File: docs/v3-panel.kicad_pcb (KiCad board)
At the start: 2 copper layers, 20 x 128.5 mm, 0 parts

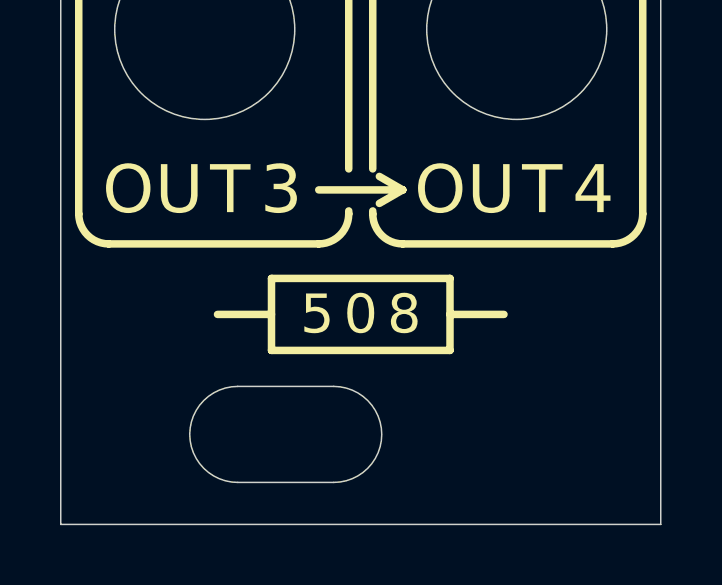
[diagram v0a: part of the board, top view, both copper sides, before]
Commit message: Add v3 DigiKey BOM and reorganize references
Add an upload-ready DigiKey BOM (docs/BOM_v3_DigiKey.csv) and update README/docs to point v2.2 artifacts into a new reference/ directory. Adjust .gitignore for the local Numbers BOM, clarify C9/C10 mounting/ESR in docs/v3-BOM.md and reconcile sourcing notes. Move existing v2.2 files (schematic, gerbers, photos, BOM) into reference/, and update docs/v2.2-topology.md. Large kicad edits to docs/v3-adder.kicad_pcb and docs/v3-panel.kicad_pcb update silk, nets and layout metadata. These changes prepare sourcing and cleanly separate the finished v2.2 reference from v3 work.
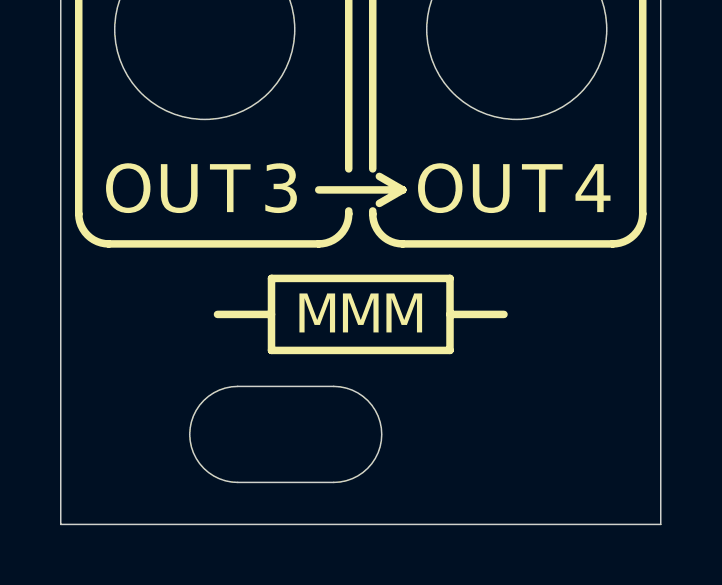
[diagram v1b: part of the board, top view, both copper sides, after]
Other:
- board text removed: "8"
